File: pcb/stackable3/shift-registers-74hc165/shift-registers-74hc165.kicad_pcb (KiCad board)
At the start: 2 copper layers, 32 x 32 mm, 38 parts, among them J1 Pin headers, J2 Pin socket, J3 Pin headers, J6 JST SH, J7 JST SH, Q1 AO3401A, SW0 SW_SPDT_MountingPin, SW1 Tactile, right-angle, SW2 Tactile 3.3mm, SW3 Tactile 3.3mm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

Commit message: Add more LCSC part numbers on stackable3/shift-registers-74hc165
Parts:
- RN1, RN2: value 1K -> 5K1
- RN3, RN4: value 1K -> 10K
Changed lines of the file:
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@@
 			)
 		)
+		(property "LCSC Part" "C110924"
+			(at 0 0 90)
+			(unlocked yes)
+			(layer "F.Fab")
+			(hide yes)
+			(effects
+				(font
+					(size 1 1)
+					(thickness 0.15)
+				)
+			)
+		)
 		(property ki_fp_filters "DIP* SOIC* R*Array*Concave* R*Array*Convex* MSOP*")
 		(sheetname "Root")
@@
 			)
 		)
-		(property "Value" "1K"
+		(property "Value" "10K"
 			(at 0 2.1 90)
 			(layer "F.Fab")
@@
 			)
 		)
+		(property "LCSC Part" "C7422173"
+			(at 0 0 -90)
+			(unlocked yes)
+			(layer "F.Fab")
+			(hide yes)
+			(effects
+				(font
+					(size 1 1)
+					(thickness 0.15)
+				)
+			)
+		)
 		(property ki_fp_filters "DIP* SOIC* R*Array*Concave* R*Array*Convex* MSOP*")
 		(sheetname "Root")
@@
 			)
 		)
-		(property "Value" "1K"
+		(property "Value" "5K1"
 			(at 0 2.1 90)
 			(layer "F.Fab")
@@
 			)
 		)
+		(property "LCSC Part" "C425290"
+			(at 0 0 90)
+			(unlocked yes)
+			(layer "F.Fab")
+			(hide yes)
+			(effects
+				(font
+					(size 1 1)
+					(thickness 0.15)
+				)
+			)
+		)
 		(property ki_fp_filters "DIP* SOIC* R*Array*Concave* R*Array*Convex* MSOP*")
 		(sheetname "Root")
@@
 			)
 		)
-		(property "Value" "1K"
+		(property "Value" "10K"
 			(at 0 2.1 90)
 			(layer "F.Fab")
@@
 			)
 		)
+		(property "LCSC Part" "C7422173"
+			(at 0 0 -90)
+			(unlocked yes)
+			(layer "F.Fab")
+			(hide yes)
+			(effects
+				(font
+					(size 1 1)
+					(thickness 0.15)
+				)
+			)
+		)
 		(property ki_fp_filters "DIP* SOIC* R*Array*Concave* R*Array*Convex* MSOP*")
 		(sheetname "Root")
@@
 			)
 		)
-		(property "Value" "1K"
+		(property "Value" "5K1"
 			(at 0 2.1 90)
 			(layer "F.Fab")
@@
 					(thickness 0.15)
 				)
+			)
+		)
+		(property "LCSC Part" "C425290"
+			(at 0 0 90)
+			(unlocked yes)
+			(layer "F.Fab")
+			(hide yes)
+			(effects
+				(font
+					(size 1 1)
+					(thickness 0.15)
+				)

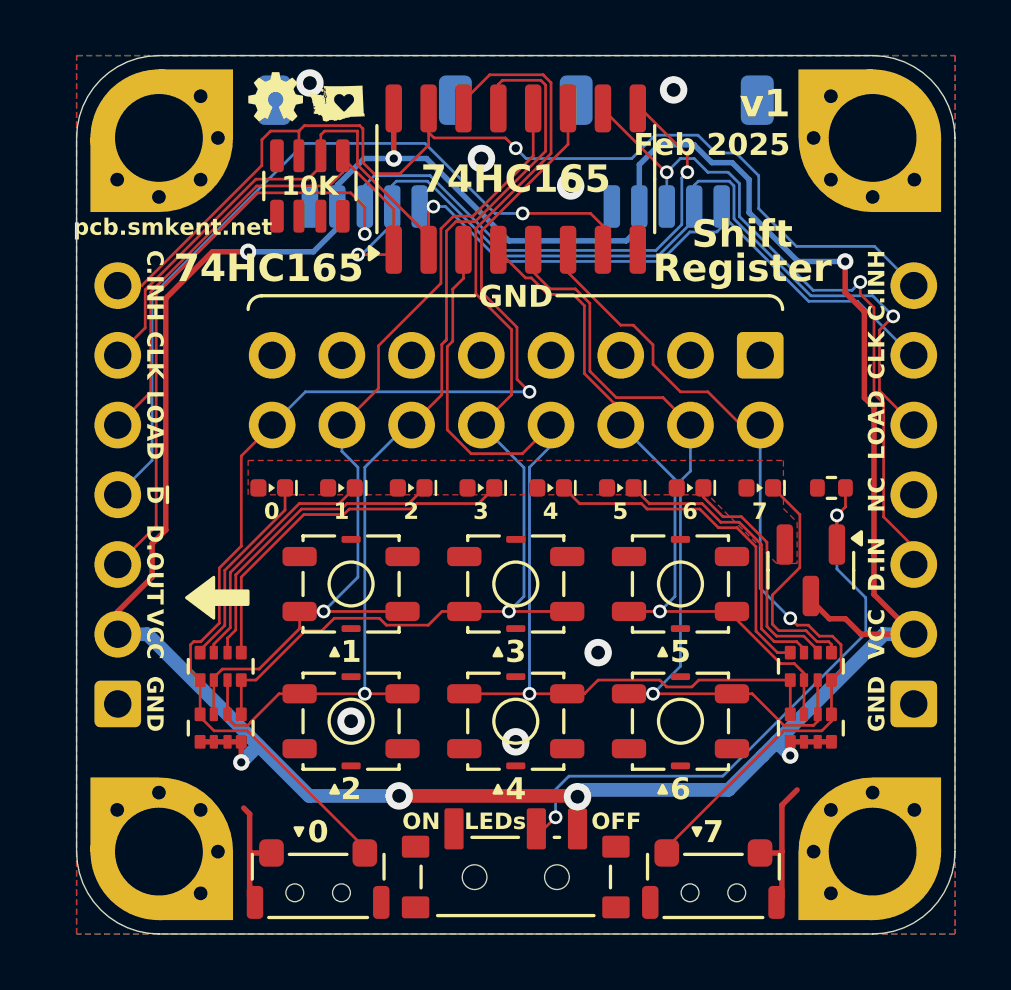
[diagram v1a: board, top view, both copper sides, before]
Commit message: Fix LEDs MOSFET direction in stackable3/shift-registers-74hc165 circuit
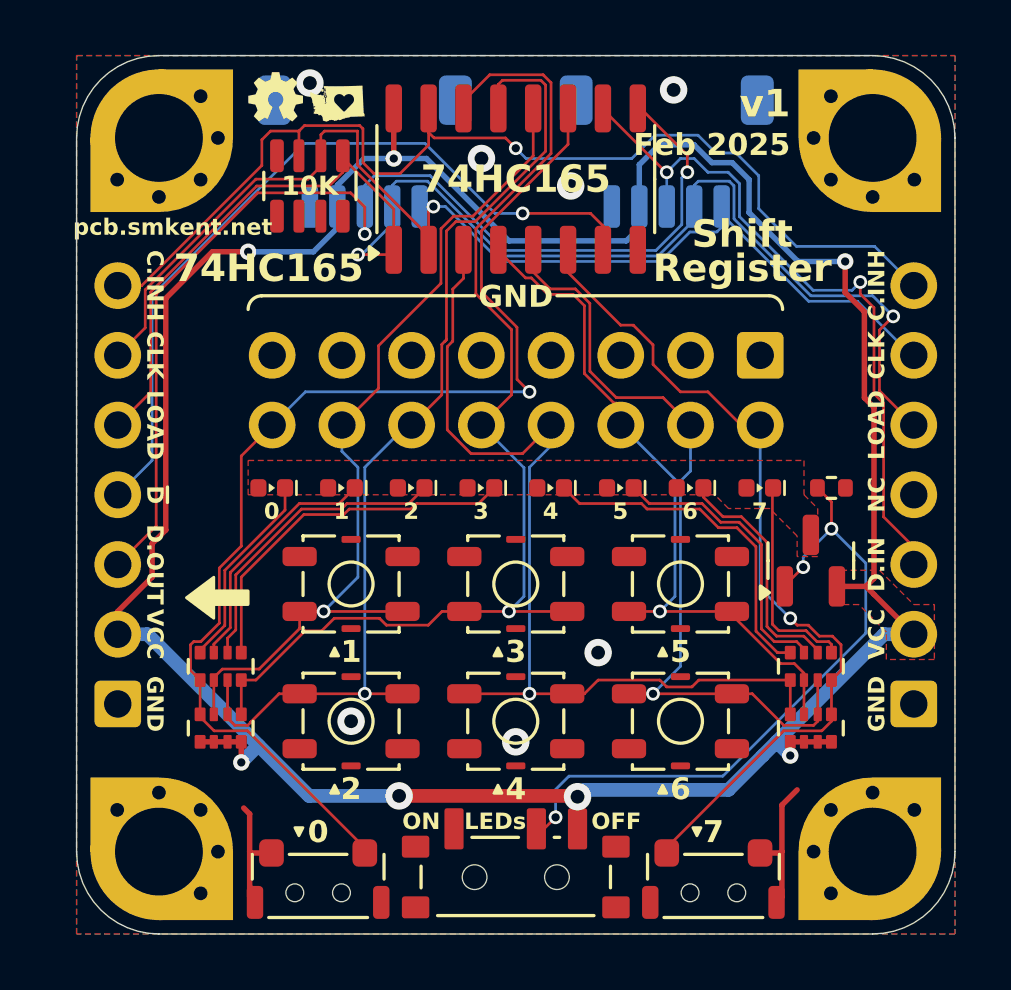
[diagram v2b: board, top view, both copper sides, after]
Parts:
- moved Q1 0.35 mm to (80.8, 38.4), turned to 90 degrees
- turned R1 to 0 degrees
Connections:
- Q1 pad 2: LED_VCC -> VCC
- Q1 pad 3: VCC -> LED_VCC
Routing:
- net VCC: track 109.0 -> 105.9 mm
- net LED_VCC_GATE_T: track 22.5 -> 24.4 mm, vias 2 -> 3
- net /LED8_K_T: track 8.54 -> 7.73 mm
- added copper zone on F.Cu, net VCC
